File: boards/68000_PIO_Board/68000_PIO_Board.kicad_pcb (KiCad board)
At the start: 2 copper layers, 101.6 x 55.9 mm, 20 parts, among them J1 Conn_02x08_Odd_Even, J10 Conn_01x08, J11 Conn_01x08, J12 Conn_01x08, J13 Conn_01x10, J2 Conn_02x08_Odd_Even, J3 Conn_02x08_Odd_Even, J4 Conn_01x03, J5 Conn_01x03, J6 Conn_02x04_Odd_Even, J7 Conn_02x04_Odd_Even, J8 Conn_02x04_Odd_Even, J9 Conn_02x04_Odd_Even, M1 RC2014_40_PIN, U1 68230, U2 68230, U3 74LS138

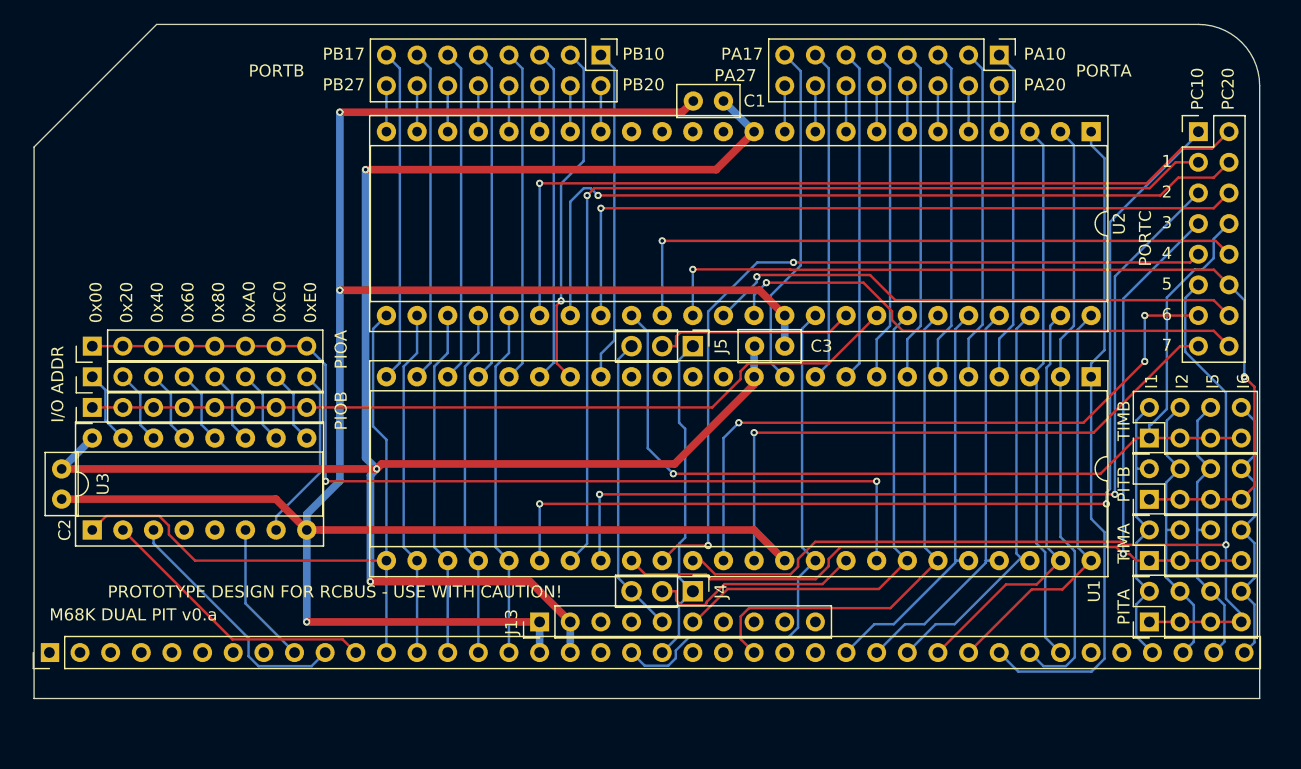
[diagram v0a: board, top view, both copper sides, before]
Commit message: Update to v2 board set
Lots of updates to reflect the new v2 boards that use the full RCBus 80 pins as well as slight modifications to the various test programs to reflect the new IO and MEM space addresses.
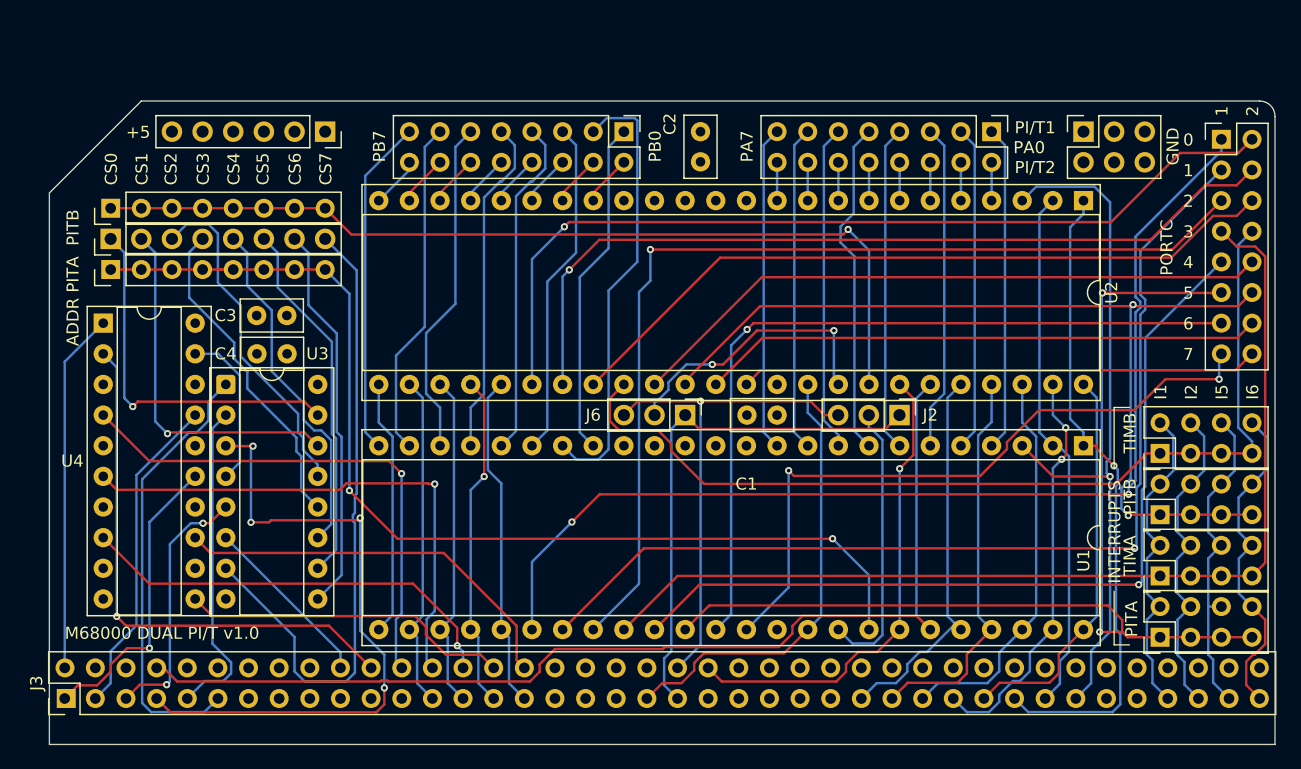
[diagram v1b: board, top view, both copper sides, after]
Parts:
- removed M1: RC2014_40_PIN, MyLibrary2023:RC2014_STD_40_PIN
- added C4: 100n, Capacitor_THT:C_Disc_D5.0mm_W2.5mm_P2.50mm, F.Cu at (144.2, 92.1)
- added J14: Conn_02x03_Odd_Even, Connector_PinSocket_2.54mm:PinSocket_2x03_P2.54mm_Vertical, F.Cu at (212.7, 73.7)
- added J15: Conn_01x06, Connector_PinSocket_2.54mm:PinSocket_1x06_P2.54mm_Vertical, F.Cu at (149.9, 73.7)
- added U4: 74LS688, MyLibrary2023:DIP-20_W7.62mm_Socket, F.Cu at (131.5, 89.5)
- J10, J11: value Conn_01x08 -> Conn_02x04_Odd_Even; footprint MyLibrary2023:PinHeader_1x08_P2.54mm_Vertical -> MyLibrary2023:PinHeader_2x04_P2.54mm_Vertical
- J13: value Conn_01x10 -> Conn_01x08; footprint MyLibrary2023:PinHeader_1x10_P2.54mm_Vertical -> MyLibrary2023:PinHeader_1x08_P2.54mm_Vertical
- J2: value Conn_02x08_Odd_Even -> Conn_01x03; footprint MyLibrary2023:PinHeader_2x08_P2.54mm_Vertical -> Connector_PinHeader_2.54mm:PinHeader_1x03_P2.54mm_Vertical
- J3: value Conn_02x08_Odd_Even -> RCBus_80PIN_68000; footprint MyLibrary2023:PinHeader_2x08_P2.54mm_Vertical -> MyLibrary2023:RCBus_80p_Medium
- J4, J5: value Conn_01x03 -> Conn_02x08_Odd_Even; footprint Connector_PinHeader_2.54mm:PinHeader_1x03_P2.54mm_Vertical -> MyLibrary2023:PinHeader_2x08_P2.54mm_Vertical
- J6: value Conn_02x04_Odd_Even -> Conn_01x03; footprint MyLibrary2023:PinHeader_2x04_P2.54mm_Vertical -> Connector_PinHeader_2.54mm:PinHeader_1x03_P2.54mm_Vertical
- J7: value Conn_02x04_Odd_Even -> Conn_01x08; footprint MyLibrary2023:PinHeader_2x04_P2.54mm_Vertical -> Connector_PinHeader_2.54mm:PinHeader_1x08_P2.54mm_Vertical
- moved J3 108.0 mm to (127.0, 124.5)
- moved J7 91.8 mm to (132.1, 82.5)
- moved J11 89.6 mm to (219.1, 105.4)
- moved J10 88.7 mm to (219.1, 100.3)
- moved C2 58.8 mm to (181.0, 76.2), turned to 90 degrees
- moved J13 49.4 mm to (132.1, 80.0)
- moved J5 47.1 mm to (224.2, 74.3), turned to 0 degrees
- moved C3 41.4 mm to (146.7, 88.9)
- moved J6 40.3 mm to (179.7, 97.2), turned to -90 degrees
- moved J2 38.8 mm to (197.5, 97.2)
- moved J4 38.5 mm to (174.6, 73.7)
- moved C1 26.1 mm to (184.8, 97.2), turned to 0 degrees
- moved U3 16.4 mm to (141.6, 94.6), turned to 0 degrees
- moved J12 11.5 mm to (132.1, 85.1)
- moved J8 11.5 mm to (219.1, 110.5)
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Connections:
- J10 pad 1: Net-(J10-Pin_1) -> /PC2_3
- J10 pad 2: Net-(J10-Pin_2) -> /~{INT1}
- J10 pad 3: Net-(J10-Pin_3) -> /PC2_3
- J10 pad 4: Net-(J10-Pin_4) -> /~{INT2}
- J10 pad 5: Net-(J10-Pin_5) -> /PC2_3
- J10 pad 6: Net-(J10-Pin_6) -> /~{INT5}
- J10 pad 7: Net-(J10-Pin_7) -> /PC2_3
- J10 pad 8: Net-(J10-Pin_8) -> /~{INT6}
- J11 pad 1: /~{PIOA_CS} -> /PC2_5
- J11 pad 2: /~{PIOA_CS} -> /~{INT1}
- J11 pad 3: /~{PIOA_CS} -> /PC2_5
- J11 pad 4: /~{PIOA_CS} -> /~{INT2}
- J11 pad 5: /~{PIOA_CS} -> /PC2_5
- J11 pad 6: /~{PIOA_CS} -> /~{INT5}
- J11 pad 7: /~{PIOA_CS} -> /PC2_5
- J11 pad 8: /~{PIOA_CS} -> /~{INT6}
- J12 pad 1: /~{PIOB_CS} -> /~{PITA_CS}
- J12 pad 2: /~{PIOB_CS} -> /~{PITA_CS}
- J12 pad 3: /~{PIOB_CS} -> /~{PITA_CS}
- J12 pad 4: /~{PIOB_CS} -> /~{PITA_CS}
- J12 pad 5: /~{PIOB_CS} -> /~{PITA_CS}
- J12 pad 6: /~{PIOB_CS} -> /~{PITA_CS}
- J12 pad 7: /~{PIOB_CS} -> /~{PITA_CS}
- J12 pad 8: /~{PIOB_CS} -> /~{PITA_CS}
- J13 pad 1: GND -> /~{PITB_CS}
- J13 pad 2: +5V -> /~{PITB_CS}
- J13 pad 3: unconnected-(J13-Pin_3-Pad3) -> /~{PITB_CS}
- J13 pad 4: unconnected-(J13-Pin_4-Pad4) -> /~{PITB_CS}
- J13 pad 5: /E -> /~{PITB_CS}
- J13 pad 6: /~{DTACK} -> /~{PITB_CS}
- J13 pad 7: unconnected-(J13-Pin_7-Pad7) -> /~{PITB_CS}
- J13 pad 8: unconnected-(J13-Pin_8-Pad8) -> /~{PITB_CS}
- J2 pad 1: /PB1_0 -> /CLOCK
- J2 pad 2: /PB2_0 -> /PITA_CLK
- J2 pad 3: /PB1_1 -> /CLOCK2
- J3 pad 1: /PC1_0 -> /A16
- J3 pad 10: /PC2_4 -> unconnected-(J3-A6-Pad10)
- J3 pad 11: /PC1_5 -> unconnected-(J3-A5-Pad11)
- J3 pad 12: /PC2_5 -> unconnected-(J3-A4-Pad12)
- J3 pad 13: /PC1_6 -> /A4
- J3 pad 14: /PC2_6 -> /A3
- J3 pad 15: /PC1_7 -> /A2
- J3 pad 16: /PC2_7 -> /A1
- J3 pad 2: /PC2_0 -> /A15
- J3 pad 3: /PC1_1 -> /A14
- J3 pad 4: /PC2_1 -> /A13
- J3 pad 5: /PC1_2 -> /A12
- J3 pad 6: /PC2_2 -> /A11
- J3 pad 7: /PC1_3 -> unconnected-(J3-A9-Pad7)
- J3 pad 8: /PC2_3 -> unconnected-(J3-A8-Pad8)
- J3 pad 9: /PC1_4 -> unconnected-(J3-A7-Pad9)
- J4 pad 1: /CLOCK -> /PB1_0
- J4 pad 2: /PIOA_CLK -> /PB2_0
- J4 pad 3: /E -> /PB1_1
- J5 pad 1: /CLOCK -> /PC1_0
- J5 pad 2: /PIOB_CLK -> /PC2_0
- J5 pad 3: /E -> /PC1_1
- J6 pad 1: /PC1_3 -> /CLOCK
- J6 pad 2: /~{INT1} -> /PITB_CLK
- J6 pad 3: /PC1_3 -> /CLOCK2
- J7 pad 1: /PC1_5 -> Net-(J7-Pin_1)
- J7 pad 2: /~{INT1} -> Net-(J7-Pin_2)
- J7 pad 3: /PC1_5 -> Net-(J7-Pin_3)
- J7 pad 4: /~{INT2} -> Net-(J7-Pin_4)
- J7 pad 5: /PC1_5 -> Net-(J7-Pin_5)
- J7 pad 6: /~{INT5} -> Net-(J7-Pin_6)
- J7 pad 7: /PC1_5 -> Net-(J7-Pin_7)
- J7 pad 8: /~{INT6} -> Net-(J7-Pin_8)
- J8 pad 1: /PC2_3 -> /PC1_3
- J8 pad 3: /PC2_3 -> /PC1_3
- J8 pad 5: /PC2_3 -> /PC1_3
- J8 pad 7: /PC2_3 -> /PC1_3
- J9 pad 1: /PC2_5 -> /PC1_5
- J9 pad 3: /PC2_5 -> /PC1_5
- J9 pad 5: /PC2_5 -> /PC1_5
- J9 pad 7: /PC2_5 -> /PC1_5
- U1 pad 40: /PIOA_CLK -> /PITA_CLK
- U1 pad 41: /~{PIOA_CS} -> /~{PITA_CS}
- U1 pad 43: /~{WR} -> /R/~{W}
- U2 pad 40: /PIOB_CLK -> /PITB_CLK
- U2 pad 41: /~{PIOB_CS} -> /~{PITB_CS}
- U2 pad 43: /~{WR} -> /R/~{W}
- U3 pad 1: /A5 -> /A11
- U3 pad 10: Net-(J10-Pin_6) -> Net-(J7-Pin_6)
- U3 pad 11: Net-(J10-Pin_5) -> Net-(J7-Pin_5)
- U3 pad 12: Net-(J10-Pin_4) -> Net-(J7-Pin_4)
- U3 pad 13: Net-(J10-Pin_3) -> Net-(J7-Pin_3)
- U3 pad 14: Net-(J10-Pin_2) -> Net-(J7-Pin_2)
- U3 pad 15: Net-(J10-Pin_1) -> Net-(J7-Pin_1)
- U3 pad 2: /A6 -> /A12
- U3 pad 3: /A7 -> /A13
- U3 pad 4: unconnected-(U3-E1-Pad4) -> Net-(U3-E1)
- U3 pad 5: /~{IORQ} -> /A14
- U3 pad 6: /A8 -> /A23
- U3 pad 7: Net-(J10-Pin_8) -> Net-(J7-Pin_8)
- U3 pad 9: Net-(J10-Pin_7) -> Net-(J7-Pin_7)
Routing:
- net GND: track 197.3 -> 0.00 mm, vias 3 -> 0
- net +5V: track 159.5 -> 0.00 mm, vias 3 -> 0
- net /R/~{W}: track 0.00 -> 88.8 mm
- net /~{PITA_CS}: track 0.00 -> 88.5 mm, vias 0 -> 2
- net /~{PIOA_CS}: track 81.9 -> 0.00 mm, vias 2 -> 0
- net /~{PITB_CS}: track 0.00 -> 75.8 mm, vias 0 -> 1
- net /~{PIOB_CS}: track 68.6 -> 0.00 mm
- net Net-(J7-Pin_8): track 0.00 -> 53.8 mm
- net /A13: track 0.00 -> 53.7 mm, vias 0 -> 4
- net /A22: track 0.00 -> 45.1 mm, vias 0 -> 1
- net /A20: track 0.00 -> 43.2 mm, vias 0 -> 1
- net /~{WR}: track 43.0 -> 0.00 mm
- net /A21: track 0.00 -> 42.6 mm, vias 0 -> 1
- net /CLOCK2: track 0.00 -> 41.6 mm, vias 0 -> 1
- net /A11: track 0.00 -> 36.7 mm
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- added copper zone on In1.Cu, net +5V
- added copper zone on In2.Cu, net GND
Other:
- board size 101.6 x 55.9 mm -> 101.6 x 53.3 mm
- copper layers 2 -> 4
- board text added: "+5"
- board text added: "+5V POWER PINS"
- board text added: "0"
- board text added: "ADDR PITA PITB"
- board text added: "CS0"
- board text added: "CS0: D08000 CS1: D08800 CS2: D09000 CS3: D09800"
- board text added: "CS1"
- board text added: "CS2"
- board text added: "CS3"
- board text added: "CS4"
- board text added: "CS4: D0A000 CS5: D0A800 CS6: D0B000 CS7: D0B800"
- board text added: "CS5"
- board text added: "CS6"
- board text added: "CS7"
- board text added: "GND"
- board text added: "GND PINS"
- board text added: "INTERRUPTS"
- board text added: "JLCJLCJLCJLC"
- board text added: "M68000 DUAL PI/T v1.0"
- board text added: "PA0"
- board text added: "PA7"
- board text added: "PB0"
- board text added: "PB7"
- board text added: "PI/T #1"
- board text added: "PI/T #1 CLK SRC"
- board text added: "PI/T #2"
- board text added: "PI/T #2 CLK SRC"
- board text added: "PI/T CLOCK SOURCES 1-2 : SYS CLOCK 2-3 : SYS E CLK OR UART CLK"
- board text added: "PI/T1"
- board text added: "PI/T2"
- board text added: "RCBUS-80 M68000 DUAL PI/T v1.0"
- board text removed: "0x00"
- board text removed: "0x20"
- board text removed: "0x40"
- board text removed: "0x60"
- board text removed: "0x80"
- board text removed: "0xA0"
- board text removed: "0xC0"
- board text removed: "0xE0"
- board text removed: "I/O ADDR"
- board text removed: "M68K DUAL PIT v0.a"
- board text removed: "PA10"
- board text removed: "PA17"
- board text removed: "PA20"
- board text removed: "PA27"
- board text removed: "PB10"
- board text removed: "PB17"
- board text removed: "PB20"
- board text removed: "PB27"
- board text removed: "PC10"
- board text removed: "PC20"
- board text removed: "PIOA"
- board text removed: "PIOB"
- board text removed: "PIT A"
- board text removed: "PIT B"
- board text removed: "PORTA"
- board text removed: "PORTB"
- board text removed: "PROTOTYPE DESIGN FOR RCBUS - USE WITH CAUTION!"
